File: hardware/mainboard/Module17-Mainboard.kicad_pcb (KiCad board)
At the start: 4 copper layers, 100 x 83 mm, 208 parts, among them IC301 LM4991MA, J301 CAT_TX, J302 CAT_RX, J401 Radio, J402 USB_C, J403 Radio_Opt, J404 Kenwood-3.5, J405 Kenwood-2.5, J406 2.54mm Header 7p, J407 KH-RJ45-58-8P8C, J408 STLink, J409 UART, J410 Speaker, J411 +12V, J412 Hirose FH12-26S-0.5SH(55), J413 Molex 532610271, Q201 MMBT3904, Q202 IRLML2244, Q301 IRLML2060, Q302 BSS138, Q303 BSS138, SW201 Tactile switch, SW202 Tactile switch, SW203 Tactile switch, SW204 Tactile switch, SW205 Tactile switch, SW206 Tactile switch, SW207 Tactile switch, SW208 Tactile switch, U201 STM32F405RGTx, U202 TPS7A2033, U203 TP6841S6, U301 MCP6002, U302 MAX9814, U401 USBLC6-2SC6, U501 MCP4551-103, U502 MCP4551-103, U503 MCP6002, U504 MCP6002, Y201 8 MHz

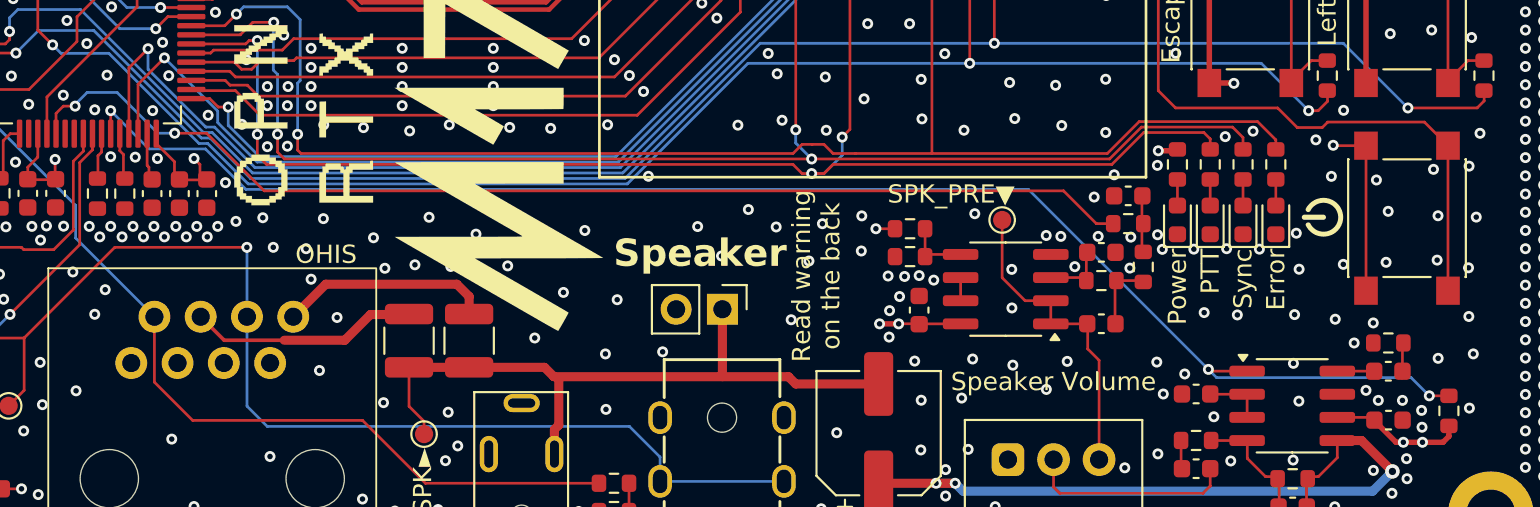
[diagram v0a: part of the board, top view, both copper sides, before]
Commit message: Added OSHWA certification mark
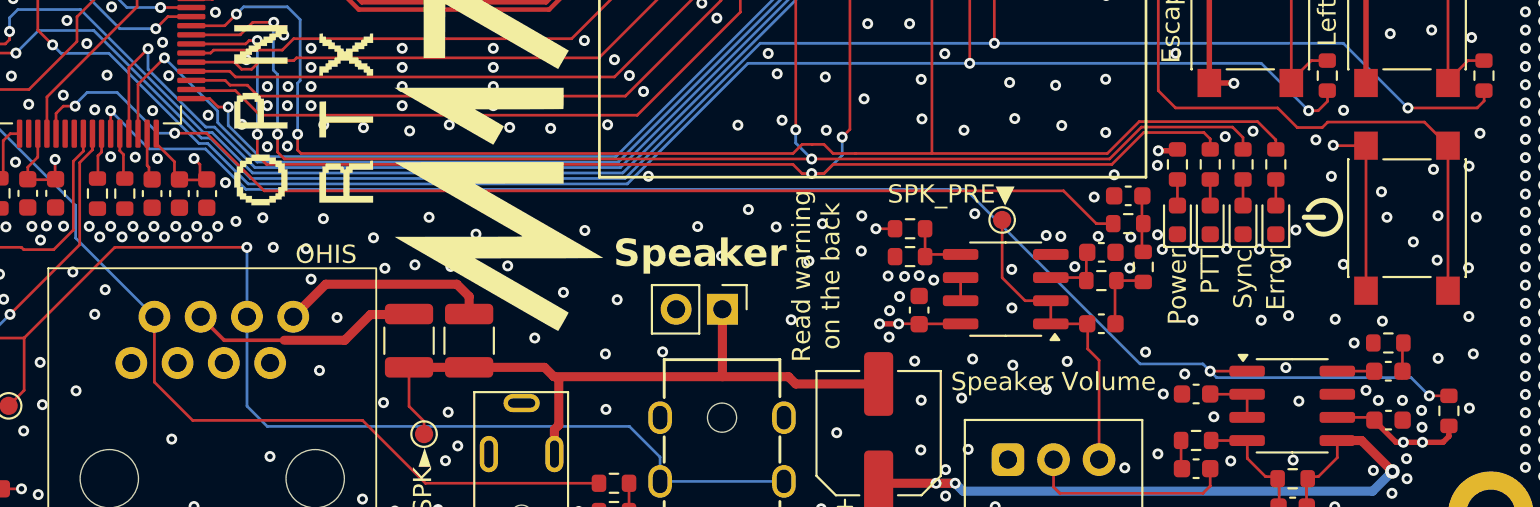
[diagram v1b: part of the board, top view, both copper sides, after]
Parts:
- removed LOGO103: OSHW_logo, M17_logos:OSHW_logo_12.5x13mm
- added LOGO104: ~, OSHW_Certification_Mark:OSHW-Certification-Mark-Stacked_12x10mm_SilkMask, B.Cu at (252.8, 112.5)

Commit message: Fixed missing symbol
Barrel polarity symbol was missing. No electrical or functional changes.
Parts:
- added REF**: Symbol_Barrel_Polarity, Symbol:Symbol_Barrel_Polarity, B.Cu at (233.8, 57.6)
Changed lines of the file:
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@@
+		)
+	)
+	(footprint "Symbol:Symbol_Barrel_Polarity"
+		(layer "B.Cu")
+		(at 233.8 57.6 180)
+		(descr "Barrel connector polarity indicator")
+		(tags "barrel polarity")
+		(property "Reference" "REF**"
+			(at 0 2 0)
+			(layer "B.SilkS")
+			(hide yes)
+			(effects
+				(font
+					(size 1 1)
+					(thickness 0.15)
+				)
+				(justify mirror)
+			)
+		)
+		(property "Value" "Symbol_Barrel_Polarity"
+			(at 0 -2 0)
+			(layer "B.Fab")
+			(effects
+				(font
+					(size 1 1)
+					(thickness 0.15)
+				)
+				(justify mirror)
+			)
+		)
+		(property "Footprint" "Symbol:Symbol_Barrel_Polarity"
+			(at 0 0 0)
+			(unlocked yes)
+			(layer "B.Fab")
+			(hide yes)
+			(effects
+				(font
+					(size 1.27 1.27)
+					(thickness 0.15)
+				)
+				(justify mirror)
+			)
+		)
+		(property "Datasheet" ""
+			(at 0 0 0)
+			(unlocked yes)
+			(layer "B.Fab")
+			(hide yes)
+			(effects
+				(font
+					(size 1.27 1.27)
+					(thickness 0.15)
+				)
+				(justify mirror)
+			)
+		)
+		(property "Description" ""
+			(at 0 0 0)
+			(unlocked yes)
+			(layer "B.Fab")
+			(hide yes)
+			(effects
+				(font
+					(size 1.27 1.27)
+					(thickness 0.15)
+				)
+				(justify mirror)
+			)
+		)
+		(attr board_only exclude_from_pos_files exclude_from_bom allow_missing_courtyard)
+		(fp_line
+			(start 2 -0.075)
+			(end 0 -0.075)
+			(stroke
+				(width 0.15)
+				(type solid)
+			)
+			(layer "B.SilkS")
+		)
+		(fp_line
+			(start -1.1 -0.075)
+			(end -2 -0.075)
+			(stroke
+				(width 0.15)
+				(type solid)
+			)
+			(layer "B.SilkS")
+		)
+		(fp_arc
+			(start 0.675 0.675)
+			(mid -1.007627 -0.128033)
+			(end 0.75 -0.75)
+			(stroke
+				(width 0.15)
+				(type solid)
+			)
+			(layer "B.SilkS")
+		)
+		(fp_circle
+			(center 3 -0.075)
+			(end 3 -1)
+			(stroke
+				(width 0.15)
+				(type solid)
+			)
+			(fill none)
+			(layer "B.SilkS")
+		)
+		(fp_circle
+			(center 0 -0.075)
+			(end 0 -0.25)
+			(stroke
+				(width 0.5)
+				(type solid)
+			)
+			(fill none)
+			(layer "B.SilkS")
+		)
+		(fp_circle
+			(center -3 -0.075)
+			(end -3 -1)
+			(stroke
+				(width 0.15)
+				(type solid)
+			)
+			(fill none)
+			(layer "B.SilkS")
 		)
 	)
